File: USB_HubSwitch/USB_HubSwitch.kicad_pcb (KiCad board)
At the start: 2 copper layers, 34.3 x 36.6 mm, 27 parts, among them J1 690-005-299-043, J2 690-005-299-043, J3 690-005-299-043, J4 M20-9990246, J5 UE27AC54100, U1 MAX40200AUK, U2 MAX40200AUK, U3 MAX40200AUK, U4 TS3USB30EDGSR

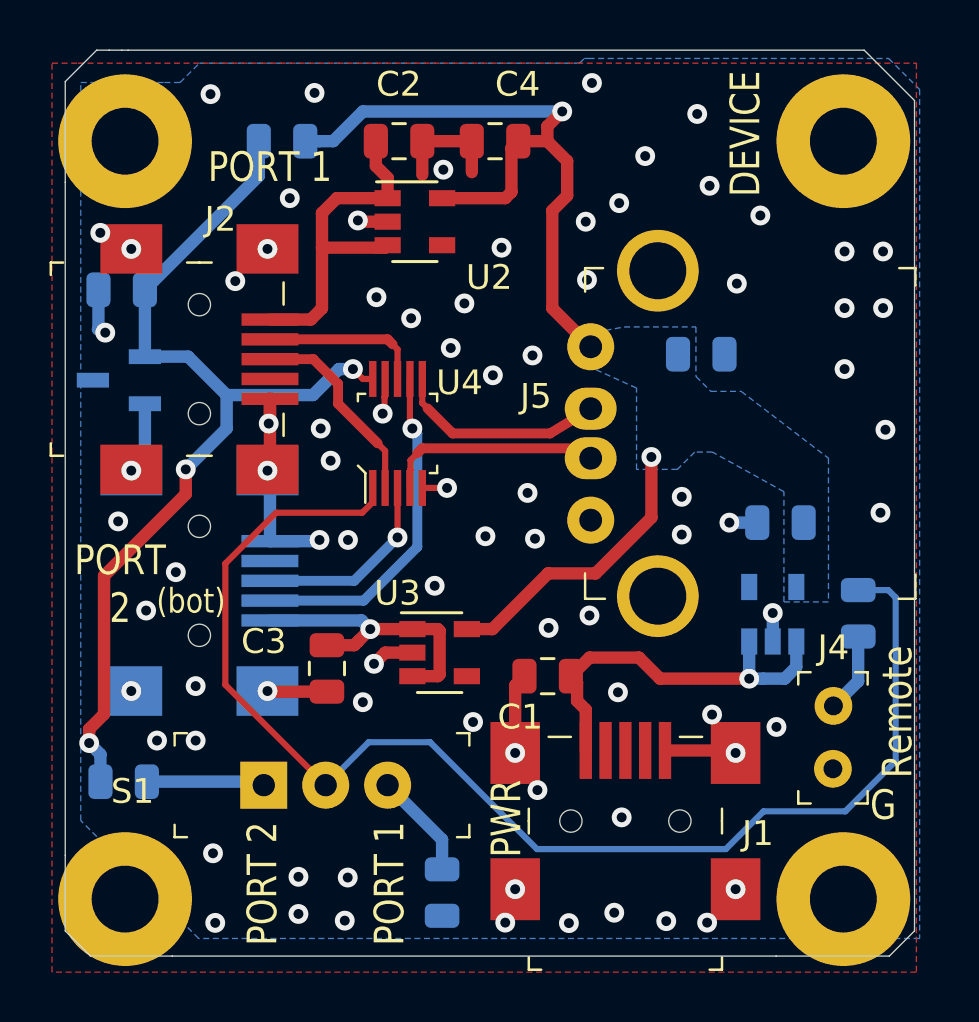
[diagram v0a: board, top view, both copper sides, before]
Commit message: Fixed USB Receptacle Pinout
this shall be used... fixed TYPE A pinout, was flipped vertically
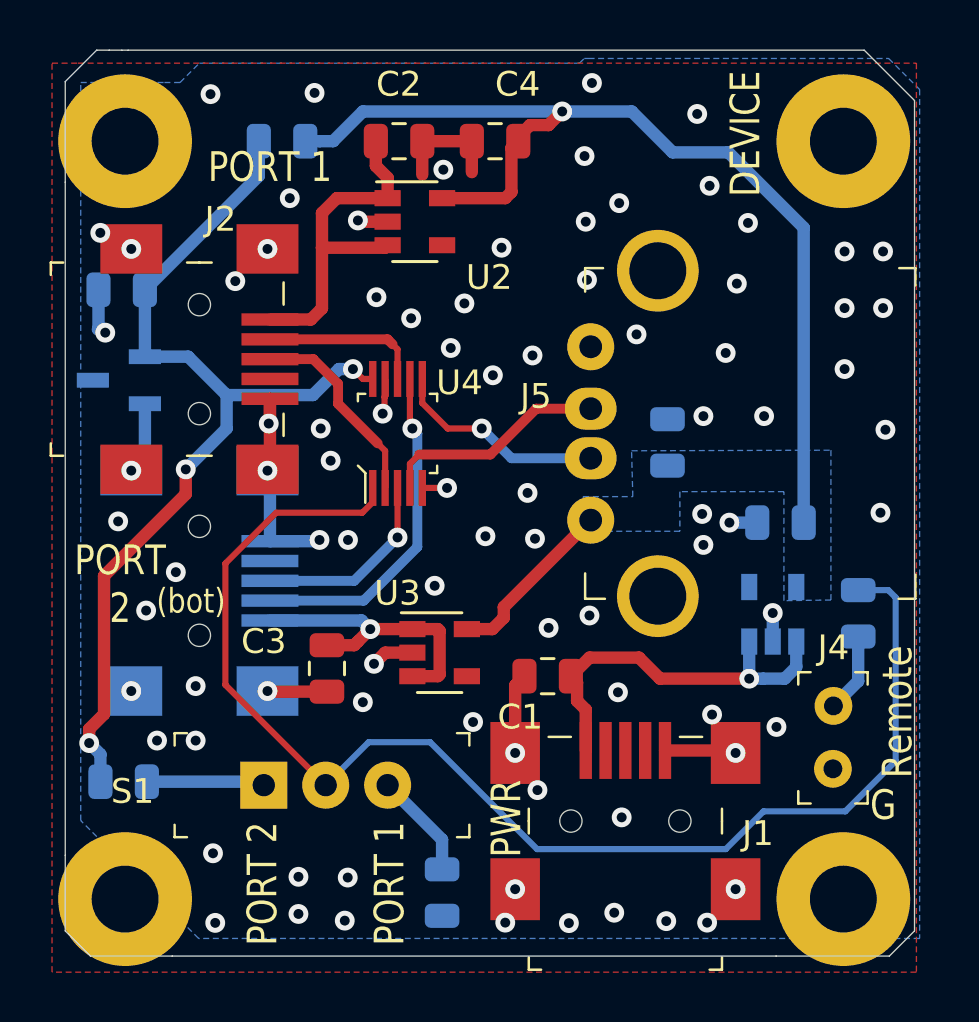
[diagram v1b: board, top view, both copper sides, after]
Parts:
- moved C7 3.81 mm to (124.9, 93.6), turned to 90 degrees
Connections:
- J5 pad 1: GNDD -> +5VD
- J5 pad 2: PORT_PERIPHERAL_DATA_P -> PORT_PERIPHERAL_DATA_N
- J5 pad 3: PORT_PERIPHERAL_DATA_N -> PORT_PERIPHERAL_DATA_P
- J5 pad 4: +5VD -> GNDD
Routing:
- net +5VD: track 39.9 -> 49.0 mm, vias 2 -> 1
- net PORT_PERIPHERAL_DATA_N: track 8.56 -> 8.70 mm, vias 0 -> 1
- net GNDD: vias 83 -> 87
